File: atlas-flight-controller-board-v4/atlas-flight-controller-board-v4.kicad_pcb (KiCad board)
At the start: 4 copper layers, 127.6 x 60 mm, 129 parts, among them IC1 LSM6DSV80XTR, J1 Conn_Coaxial, J2 Conn_Coaxial, J3 Batt Conn, J3 Conn_Coaxial, J4 DX07S016JA1R1500, J5 SWD_TC2030-NL, J6 Screw_Terminal_01x06, J7 Conn_01x02, J8 Conn_01x08, Q12 BSS138, SW3 SW_Push, SW4 HARD_RESET, U1 LIS2MDL, U10 USBLC6, U11 VNQ7140AJTR, U2 INA260, U3 SAM-M10Q-00B, U4 Value, U5 TPS62912, U6 TPS2116DRL, U7 TPS7A2133PQWDSGRQ1, U8 STM32F405RGTx, Y1 16 MHz

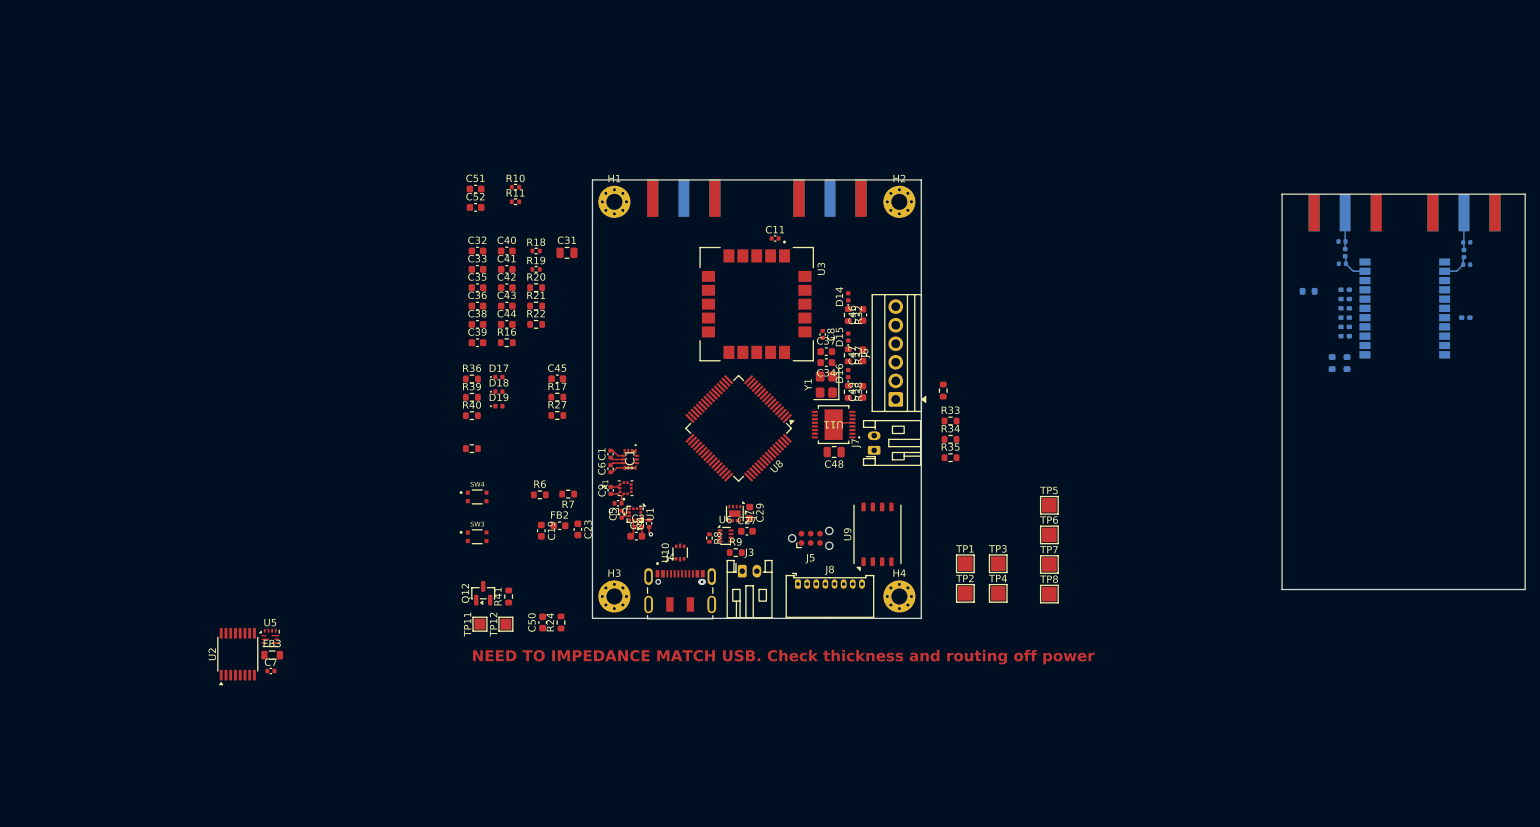
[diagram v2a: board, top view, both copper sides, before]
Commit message: progress update. schematic has been done, layout is half finished. board is now 50x65mm for rf performance reasons
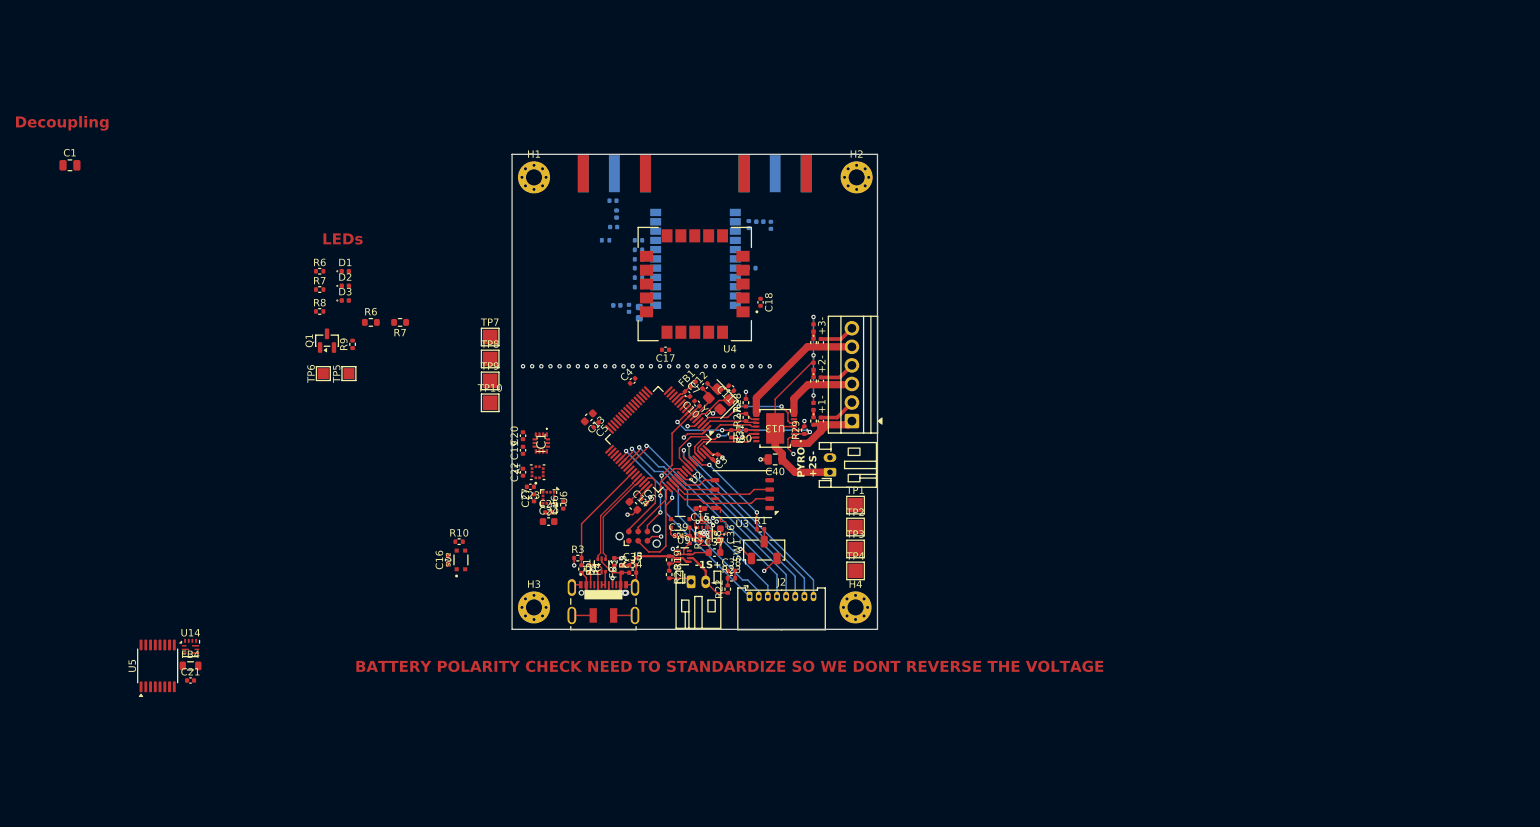
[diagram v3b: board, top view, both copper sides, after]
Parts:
- removed the C19 at (103.0, 88.0)
- removed the C23 at (108.0, 87.8)
- removed the C32 at (94.3, 49.7)
- removed the C33 at (94.3, 52.2)
- removed the C36 at (94.3, 57.3)
- removed the C40 at (98.3, 49.7)
- removed the C41 at (98.3, 52.2)
- removed the C42 at (98.3, 54.8)
- removed the C43 at (98.3, 57.3)
- removed C44, C45, C50: 100nF, Capacitor_SMD:C_0603_1608Metric
- removed C51, C52: 2u2, Capacitor_SMD:C_0603_1608Metric
- removed the J2 at (142.5, 42.5)
- removed the J3 at (122.5, 42.5)
- removed the R11 at (99.5, 43.0)
- removed the R16 at (98.3, 62.3)
- removed the R17 at (105.2, 69.7)
- removed the R18 at (102.3, 49.7)
- removed the R19 at (102.3, 52.2)
- removed the R20 at (102.3, 54.8)
- removed the R24 at (105.7, 100.6)
- removed the R27 at (105.2, 72.2)
- removed R44: 330, PCM_SparkFun-Resistor:R_0603_1608Metric
- removed SW4: HARD_RESET, myButtons:SW_USLPT2819DT2TR
- added C10: 100n, Capacitor_SMD:C_0402_1005Metric, F.Cu at (124.3, 70.6)
- added C13: 2u2, Capacitor_SMD:C_0603_1608Metric, F.Cu at (109.5, 72.5)
- added C14: 2u2, Capacitor_SMD:C_0603_1608Metric, F.Cu at (115.6, 84.6)
- added C15: 100n, Capacitor_SMD:C_0402_1005Metric_Pad0.74x0.62mm_HandSolder, F.Cu at (124.8, 85.0)
- added C16: 100n, Capacitor_SMD:C_0402_1005Metric_Pad0.74x0.62mm_HandSolder, F.Cu at (90.2, 92.0)
- added C3: 100n, Capacitor_SMD:C_0402_1005Metric, F.Cu at (126.8, 77.9)
- added C34: 100n, Capacitor_SMD:C_0402_1005Metric, F.Cu at (115.5, 93.8)
- added C4: 100n, Capacitor_SMD:C_0402_1005Metric, F.Cu at (115.5, 67.5)
- added C5: 100n, Capacitor_SMD:C_0402_1005Metric, F.Cu at (110.5, 73.5)
- added C6: 100n, Capacitor_SMD:C_0402_1005Metric, F.Cu at (117.0, 84.0)
- added C7: 100n, Capacitor_SMD:C_0402_1005Metric, F.Cu at (123.0, 69.3)
- added FB1: 120R @ 100 MHz, Inductor_SMD:L_0402_1005Metric, F.Cu at (123.7, 68.0)
- added FB3: 120R @ 100 MHz, Inductor_SMD:L_0402_1005Metric, F.Cu at (114.0, 93.2)
- added R1: 10k, Resistor_SMD:R_0402_1005Metric, F.Cu at (133.0, 87.8)
- added R2: 33k, Resistor_SMD:R_0402_1005Metric, F.Cu at (108.5, 93.2)
- added R23: 100k, Resistor_SMD:R_0402_1005Metric, F.Cu at (129.0, 94.5)
- added R3: 82k, Resistor_SMD:R_0402_1005Metric, F.Cu at (108.0, 91.8)
- added R30: 330, Resistor_SMD:R_0402_1005Metric, F.Cu at (130.5, 74.2)
- added R4: 5k1, Resistor_SMD:R_0402_1005Metric, F.Cu at (109.5, 93.2)
- added R5: 5k1, Resistor_SMD:R_0402_1005Metric, F.Cu at (113.0, 92.2)
- added SW1: SW_SPDT, Button_Switch_SMD:Nidec_Copal_CAS-120A, F.Cu at (133.5, 90.7)
- added SW2: SW_Push, myButtons:SW_USLPT2819DT2TR, F.Cu at (92.0, 92.0)
- C11: renamed from C34; value 10 pF -> 10p; footprint Capacitor_SMD:C_0603_1608Metric -> Capacitor_SMD:C_0402_1005Metric
- C12: renamed from C37; value 10 pF -> 10p; footprint Capacitor_SMD:C_0603_1608Metric -> Capacitor_SMD:C_0402_1005Metric
- C17: renamed from C8; value 0.1uF -> 100n
- C18: renamed from C11; value 0.1uF -> 100n
- C19: renamed from C6; value 100 nF -> 100n
- C20: renamed from C1; value 100 nF -> 100n
- C21: renamed from C7; value 100 nF -> 100n
- C22: renamed from C9; value 100 nF -> 100n
- C23: renamed from C10; value 100 nF -> 100n
- C24: renamed from C2; value 10uF -> 10u
- C25: renamed from C3; value 100nF -> 100n
- C26: renamed from C4; value 100nF -> 100n
- C27: renamed from C5; value 220nF -> 220n
- C32: renamed from C14; footprint Resistor_SMD:R_0603_1608Metric -> Capacitor_SMD:C_0402_1005Metric
- C33: renamed from C15; footprint Resistor_SMD:R_0603_1608Metric -> Capacitor_SMD:C_0603_1608Metric
- C35, C38, C39: value 100 nF -> 100n; footprint Capacitor_SMD:C_0603_1608Metric -> Capacitor_SMD:C_0402_1005Metric
- C36: renamed from C29; value 1uF -> 1u
- C37: renamed from C27; value 1uF -> 1u
- C41: renamed from C46; footprint Capacitor_SMD:C_0603_1608Metric -> Capacitor_SMD:C_0402_1005Metric
- C42: renamed from C47; footprint Capacitor_SMD:C_0603_1608Metric -> Capacitor_SMD:C_0402_1005Metric
- C43: renamed from C49; footprint Capacitor_SMD:C_0603_1608Metric -> Capacitor_SMD:C_0402_1005Metric
- FB2: value 100R @ 100 MHz -> 120R @ 100 MHz; footprint Inductor_SMD:L_0603_1608Metric -> Inductor_SMD:L_0402_1005Metric; moved to B.Cu
- R10: value 15k4 -> 10k
- R11: renamed from R2; footprint Capacitor_SMD:C_0402_1005Metric_Pad0.74x0.62mm_HandSolder -> Resistor_SMD:R_0402_1005Metric
- R12: renamed from R3; footprint Capacitor_SMD:C_0402_1005Metric_Pad0.74x0.62mm_HandSolder -> Resistor_SMD:R_0402_1005Metric
- R13: renamed from R4; footprint Capacitor_SMD:C_0402_1005Metric_Pad0.74x0.62mm_HandSolder -> Resistor_SMD:R_0402_1005Metric
- R14: renamed from R1; footprint Capacitor_SMD:C_0402_1005Metric_Pad0.74x0.62mm_HandSolder -> Resistor_SMD:R_0402_1005Metric
- R15: renamed from R5; footprint Capacitor_SMD:C_0402_1005Metric_Pad0.74x0.62mm_HandSolder -> Resistor_SMD:R_0402_1005Metric
- R16: renamed from R6; footprint Capacitor_SMD:C_0402_1005Metric_Pad0.74x0.62mm_HandSolder -> Resistor_SMD:R_0402_1005Metric
- R17: renamed from R7; footprint Capacitor_SMD:C_0402_1005Metric_Pad0.74x0.62mm_HandSolder -> Resistor_SMD:R_0402_1005Metric
- R18: renamed from R26; footprint Resistor_SMD:R_0603_1608Metric -> Resistor_SMD:R_0402_1005Metric
- R20: renamed from R9; footprint Resistor_SMD:R_0603_1608Metric -> Resistor_SMD:R_0402_1005Metric
- R21: value 5k1 -> 10k; footprint Resistor_SMD:R_0603_1608Metric -> Resistor_SMD:R_0402_1005Metric
- R22: value 10k -> 33k; footprint Resistor_SMD:R_0603_1608Metric -> Resistor_SMD:R_0402_1005Metric
- R24: renamed from R32; footprint Resistor_SMD:R_0603_1608Metric -> Resistor_SMD:R_0402_1005Metric
- R25: renamed from R37; footprint Resistor_SMD:R_0603_1608Metric -> Resistor_SMD:R_0402_1005Metric
- R26: renamed from R38; footprint Resistor_SMD:R_0603_1608Metric -> Resistor_SMD:R_0402_1005Metric
- R27: renamed from R33; footprint Resistor_SMD:R_0603_1608Metric -> Resistor_SMD:R_0402_1005Metric
- R28: renamed from R34; footprint Resistor_SMD:R_0603_1608Metric -> Resistor_SMD:R_0402_1005Metric
- R29: renamed from R35; footprint Resistor_SMD:R_0603_1608Metric -> Resistor_SMD:R_0402_1005Metric
- R31: renamed from R43; footprint PCM_SparkFun-Resistor:R_0603_1608Metric -> Resistor_SMD:R_0402_1005Metric
- R6: renamed from R36; footprint Resistor_SMD:R_0603_1608Metric -> Resistor_SMD:R_0402_1005Metric
- R7: renamed from R39; footprint Resistor_SMD:R_0603_1608Metric -> Resistor_SMD:R_0402_1005Metric
- R8: renamed from R40; footprint Resistor_SMD:R_0603_1608Metric -> Resistor_SMD:R_0402_1005Metric
- R9: renamed from R41; footprint Resistor_SMD:R_0603_1608Metric -> Resistor_SMD:R_0402_1005Metric
- SW3: value SW_Push -> HARD_RESET
- moved J5 100.1 mm to (113.0, 39.1)
- moved C31 99.9 mm to (112.8, 42.9)
- moved C30 99.8 mm to (112.9, 46.5)
- moved L2 99.8 mm to (113.3, 44.7)
- moved C29 98.4 mm to (131.4, 46.1), turned to -90 degrees
- moved R14 97.9 mm to (131.8, 52.1)
- moved U7 97.3 mm to (124.8, 39.4)
- moved C33 97.1 mm to (116.4, 58.2)
- moved R15 96.9 mm to (116.3, 52.1)
- moved R11 96.9 mm to (116.3, 48.3)
- moved R16 96.9 mm to (116.3, 53.4)
- moved R12 96.9 mm to (116.3, 49.6)
- moved R17 96.9 mm to (116.3, 54.7)
- moved R13 96.9 mm to (116.3, 50.9)
- moved C32 96.5 mm to (115.0, 57.6)
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- renumbered C31 to C1, C12 to C28, C13 to C29, C16 to C30, C17 to C31, C48 to C40, D17 to D1, D18 to D2, D19 to D3, D14 to D5, D15 to D6, D16 to D7, FB3 to FB4, J4 to J1, J8 to J2, J5 to J3, J1 to J4, J2 to J5, J3 to J6, J6 to J8, Q12 to Q1, R8 to R19, TP8 to TP10, TP12 to TP5, TP11 to TP6, TP5 to TP7, TP6 to TP8, TP7 to TP9, U10 to U1, U11 to U13, U5 to U14, U8 to U2, U9 to U3, U3 to U4, U2 to U5, U1 to U6, U4 to U7, U7 to U8, U6 to U9
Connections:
- net <NO NET> renamed PYRO_BATT
- C32 pad 1: Net-(U4-VCC_IN) -> Net-(U7-VCC_IN)
- C33 pad 1: Net-(U4-VCC_IN) -> Net-(U7-VCC_IN)
- C35 pad 1: +3V3 -> Net-(U9-MODE)
- C38 pad 1: +3V3 -> BATT_SENSE
- C39 pad 1: +3V3 -> GND
- C39 pad 2: GND -> Net-(U8-EN)
- FB2 pad 1: VBUS -> Net-(U7-VCC_IN)
- FB2 pad 2: Net-(U6-MODE) -> +3V3
- H1 pad 1: (no net) -> GND
- H2 pad 1: (no net) -> GND
- H3 pad 1: (no net) -> GND
- H4 pad 1: (no net) -> GND
- J1 pad 3: Net-(J4-CC1) -> Net-(J1-CC1)
- J1 pad 9: Net-(J4-CC2) -> Net-(J1-CC2)
- R10 pad 1: +3V7 -> STANDBY_TOGGLE
- R10 pad 2: Net-(U5-FB) -> Net-(C16-Pad2)
- R19 pad 1: Net-(U6-MODE) -> Net-(U9-MODE)
- R21 pad 1: GND -> Net-(U8-EN)
- R21 pad 2: Net-(J4-CC2) -> /power/MUX OUT
- R22 pad 1: STANDBY_TOGGLE -> /power/VBATT+
- R22 pad 2: Net-(C44-Pad2) -> BATT_SENSE
- SW3 pad 1: Net-(C44-Pad2) -> Net-(U8-EN)
- U14 pad 9: Net-(U5-FB) -> Net-(U14-FB)
- U2 pad 57: PYRO_SEL1 -> PYRO_SEL0
- U2 pad 62: PYRO_SEL0 -> PYRO_SEL1
- U7 pad 1: Net-(U4-VCC_IN) -> Net-(U7-VCC_IN)
- U8 pad 5: Net-(U7-EN) -> Net-(U8-EN)
- U9 pad 3: Net-(U6-MODE) -> Net-(U9-MODE)
- U9 pad 5: Net-(U6-MODE) -> Net-(U9-MODE)
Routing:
- net GND: track 10.8 -> 69.1 mm, vias 1 -> 49
- net PYRO_BATT: track 2.68 -> 39.7 mm, vias 0 -> 3
- net PWM_MOTOR_4: track 0.00 -> 32.1 mm, vias 0 -> 1
- net PWM_MOTOR_3: track 0.00 -> 31.3 mm, vias 0 -> 1
- net PWM_MOTOR_2: track 0.00 -> 31.0 mm, vias 0 -> 1
- net EXT_SDA: track 0.00 -> 30.4 mm, vias 0 -> 1
- net EXT_SCL: track 0.00 -> 29.3 mm, vias 0 -> 1
- net PWM_MOTOR_1: track 0.00 -> 28.4 mm, vias 0 -> 1
- net NRST: track 0.00 -> 27.0 mm, vias 0 -> 2
- net CAMERA_POWER_SWITCH: track 0.00 -> 23.7 mm, vias 0 -> 1
- net MOTOR_POWER_SWITCH: track 0.00 -> 23.0 mm, vias 0 -> 1
- net PYRO_1: track 0.00 -> 20.7 mm, vias 0 -> 2
- net /stm32/USB_DP-: track 0.00 -> 18.0 mm
- net Net-(J8-Pin_5): track 1.16 -> 18.2 mm
- net PYRO_2: track 0.00 -> 16.2 mm, vias 0 -> 2
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- added copper zone on F.Cu, net +3V3
- added copper zone on In2.Cu, net +3V3
- added copper zone on F.Cu, net GND
- added copper zone on In1.Cu, net GND
- added copper zone on In2.Cu, net GND
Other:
- board size 127.6 x 60 mm -> 50 x 65 mm
- board text added: "+1-"
- board text added: "+2-"
- board text added: "+3-"
- board text added: "-1S+"
- board text added: "BATTERY POLARITY CHECK NEED TO STANDARDIZE SO WE DONT REVERSE THE VOLTAGE"
- board text added: "Decoupling"
- board text added: "LEDs"
- board text added: "PYRO +2S-"
- board text removed: "NEED TO IMPEDANCE MATCH USB. Check thickness and routing off power"
